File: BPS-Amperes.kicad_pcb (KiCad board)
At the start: 2 copper layers, 58.2 x 30.2 mm, 32 parts, among them J1 ShuntConn, J2 LeaderConn, U1 AS8510-ASSM, U2 RO-123.3S_HP, U3 LTC6820, U4 HX1188FNL

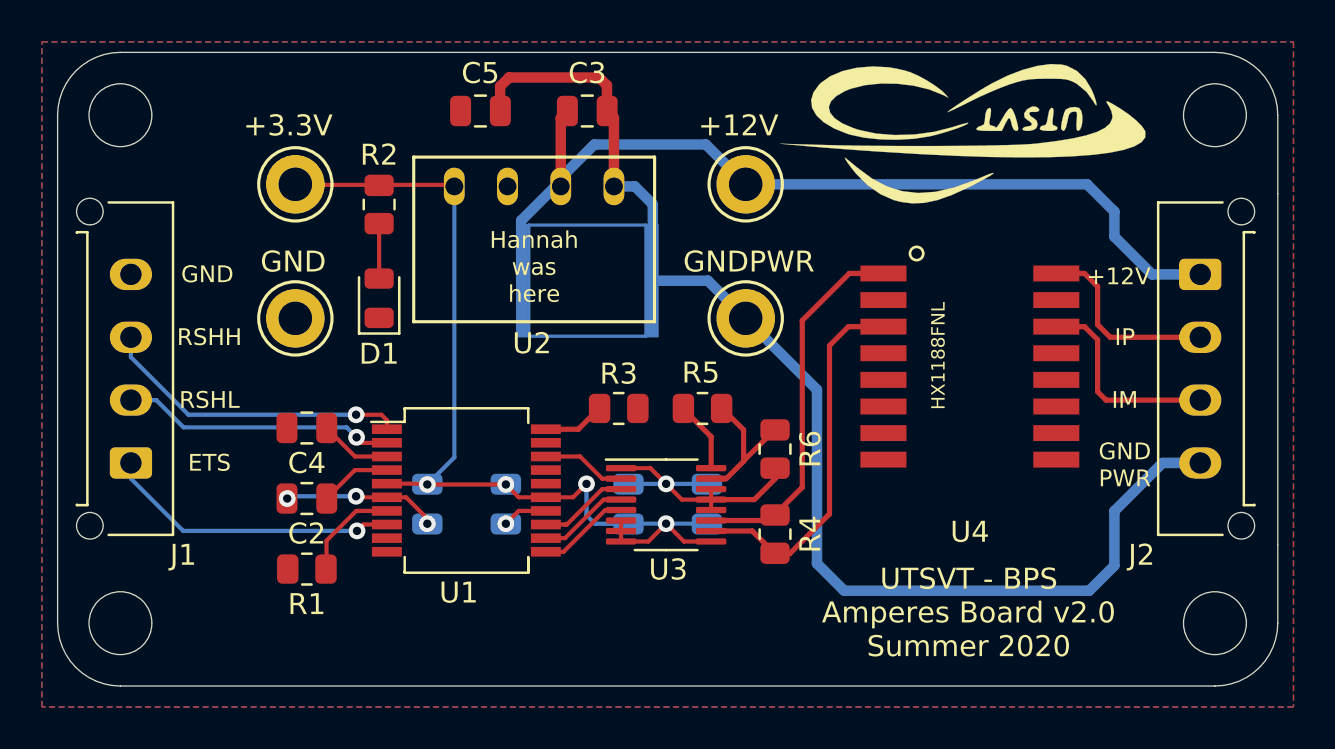
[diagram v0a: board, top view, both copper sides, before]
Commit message: Fix timing configuration issue
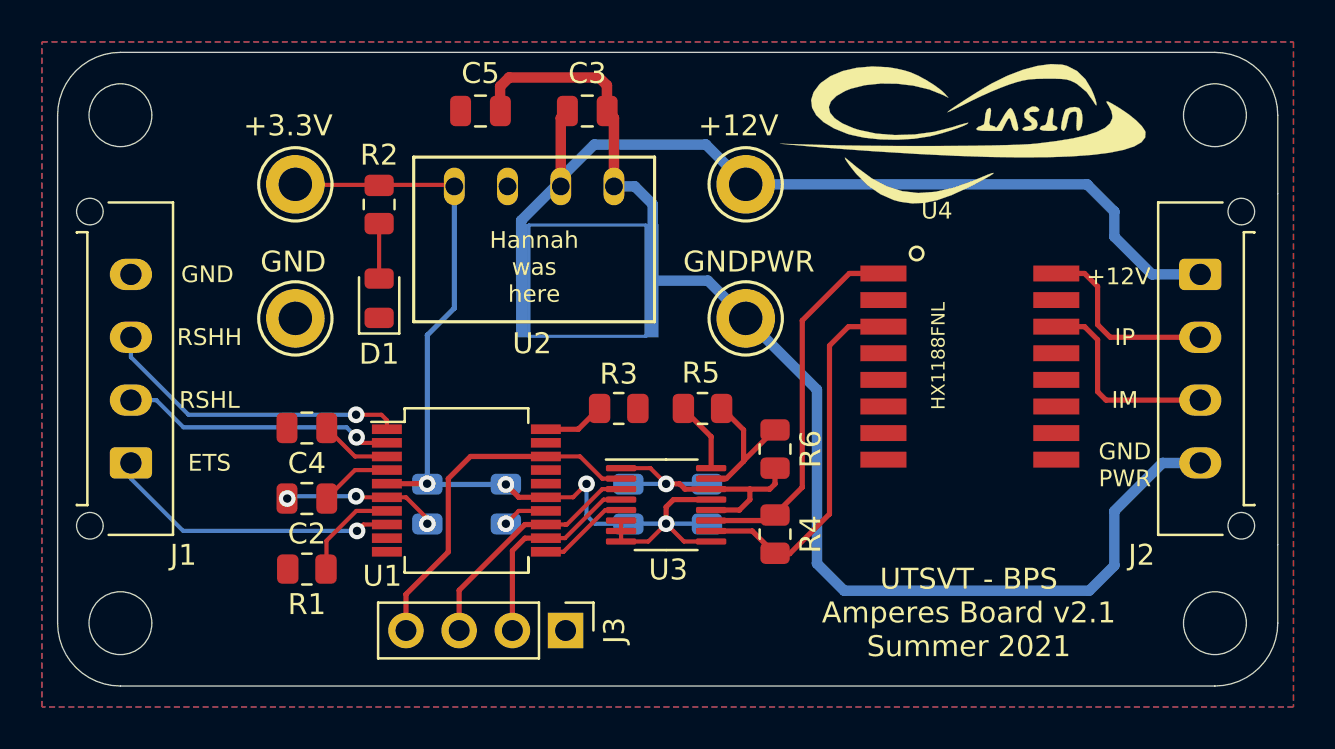
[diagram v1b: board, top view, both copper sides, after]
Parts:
- added J3: Conn_01x04, Connector_PinHeader_2.54mm:PinHeader_1x04_P2.54mm_Vertical, F.Cu at (112.0, 124.6)
- U4: footprint UTSVT_BPS:HXXXX -> UTSVT_Passive:HXXXX
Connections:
- U1 pad 10: Net-(U1-Pad10) -> (no net)
- U1 pad 16: Net-(U1-Pad16) -> (no net)
- U1 pad 17: Net-(U1-Pad17) -> (no net)
- U1 pad 19: Net-(U1-Pad19) -> (no net)
- U1 pad 9: Net-(U1-Pad9) -> (no net)
- U3 pad 13: GND -> +3V3
- U4 pad 10: Net-(U4-Pad10) -> (no net)
- U4 pad 11: Net-(U4-Pad11) -> (no net)
- U4 pad 15: Net-(U4-Pad15) -> (no net)
- U4 pad 2: Net-(U4-Pad2) -> (no net)
- U4 pad 6: Net-(U4-Pad6) -> (no net)
- U4 pad 7: Net-(U4-Pad7) -> (no net)
- U4 pad 8: Net-(U4-Pad8) -> (no net)
- U4 pad 9: Net-(U4-Pad9) -> (no net)
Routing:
- net /MOSI: track 4.03 -> 17.2 mm
- net /MISO: track 4.29 -> 11.7 mm
- net /SCK: track 4.35 -> 10.0 mm
- net +3V3: track 45.9 -> 49.0 mm
- net GND: track 23.2 -> 24.5 mm
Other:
- board text added: "UTSVT - BPS Amperes Board v2.1 Summer 2021"
- board text removed: "UTSVT - BPS Amperes Board v2.0 Summer 2020"
